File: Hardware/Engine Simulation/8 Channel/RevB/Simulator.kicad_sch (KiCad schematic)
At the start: 69 parts, among them IC1 EL357NB_TA_-G, IC2 EL357NB_TA_-G, J1 Conn_02x20_Counter_Clockwise, J2 Conn_01x08, J3 Conn_01x08, J4 Conn_01x04, J5 Conn_01x04, J6 Conn_01x04, J7 Conn_01x10, J8 Conn_01x03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

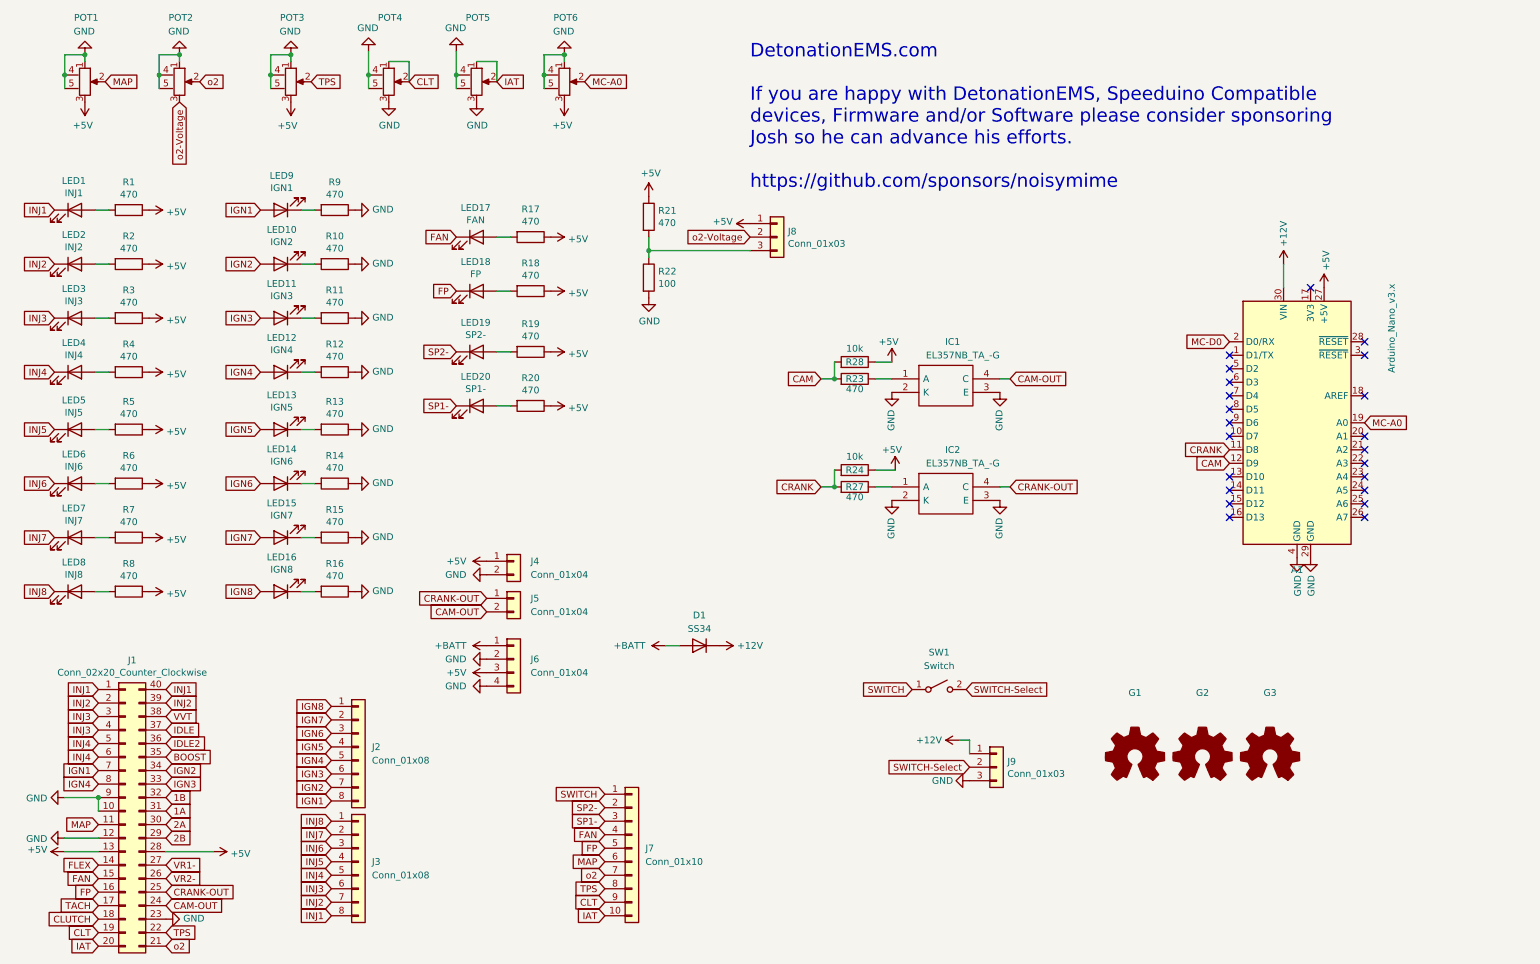
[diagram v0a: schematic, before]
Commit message: Engine Simulator Upload Revision Correcton
Minor changes were made to RevB and uploaded as RevC by mistake. RevB minor layout changes for ease of use. Protection Zener added. Label correction.
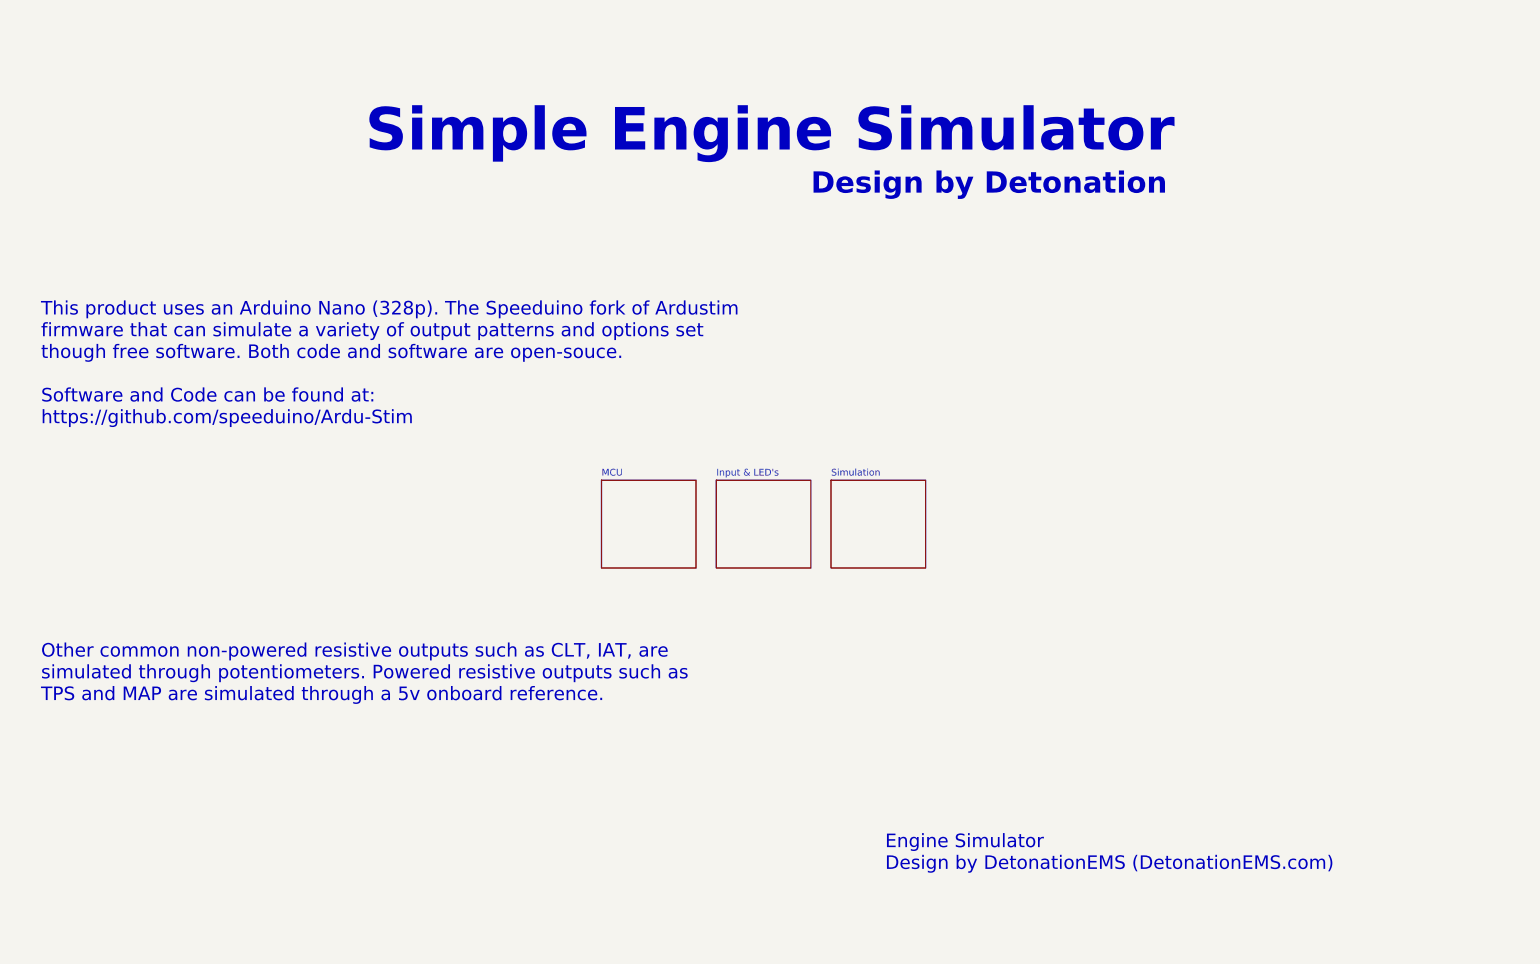
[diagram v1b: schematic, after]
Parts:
- removed A1: Arduino_Nano_v3.x, Module:Arduino_Nano, symbol MCU_Module:Arduino_Nano_v3.x
- removed D1: SS34, Diode_SMD:D_SOD-123, symbol Device:D
- removed G1: Logo_Open_Hardware_Small, Detonation-Logos:Design by 30mm, symbol Graphic:Logo_Open_Hardware_Small
- removed G2: Logo_Open_Hardware_Small, Detonation-Logos:SpeeduinoCompatible-17mm, symbol Graphic:Logo_Open_Hardware_Small
- removed G3: Logo_Open_Hardware_Small, Symbol:OSHW-Logo2_7.3x6mm_SilkScreen, symbol Graphic:Logo_Open_Hardware_Small
- removed IC1, IC2: EL357NB_TA_-G, Detonation:SOP254P700X200-4N, symbol EL357NB_TA_-G:EL357NB_TA_-G
- removed J1: Conn_02x20_Counter_Clockwise, Connector_Automotive:IDC-Header_2x20_P2.54mm_Vertical_Speeduino, symbol Pre_Ignition-rescue:Conn_02x20_Counter_Clockwise-Connector_Generic
- removed J2, J3: Conn_01x08, TerminalBlock_Phoenix:TerminalBlock_Phoenix_PT-1,5-8-3.5-H_1x08_P3.50mm_Horizontal, symbol Connector_Generic:Conn_01x08
- removed J4, J5: Conn_01x04, TerminalBlock_Phoenix:TerminalBlock_Phoenix_PT-1,5-2-3.5-H_1x02_P3.50mm_Horizontal, symbol Connector_Generic:Conn_01x02
- removed J6: Conn_01x04, TerminalBlock_Phoenix:TerminalBlock_Phoenix_PT-1,5-4-3.5-H_1x04_P3.50mm_Horizontal, symbol Connector_Generic:Conn_01x04
- removed J7: Conn_01x10, TerminalBlock_Phoenix:TerminalBlock_Phoenix_PT-1,5-10-3.5-H_1x10_P3.50mm_Horizontal, symbol Connector_Generic:Conn_01x10
- removed J8, J9: Conn_01x03, Detonation:3-PinSwitch, symbol Connector_Generic:Conn_01x03
- removed LED1: INJ1, LED_SMD:LED_0603_1608Metric, symbol Device:LED
- removed LED10: IGN2, LED_SMD:LED_0603_1608Metric, symbol Device:LED
- removed LED11: IGN3, LED_SMD:LED_0603_1608Metric, symbol Device:LED
- removed LED12: IGN4, LED_SMD:LED_0603_1608Metric, symbol Device:LED
- removed LED13: IGN5, LED_SMD:LED_0603_1608Metric, symbol Device:LED
- removed LED14: IGN6, LED_SMD:LED_0603_1608Metric, symbol Device:LED
- removed LED15: IGN7, LED_SMD:LED_0603_1608Metric, symbol Device:LED
- removed LED16: IGN8, LED_SMD:LED_0603_1608Metric, symbol Device:LED
- removed LED17: FAN, LED_SMD:LED_0603_1608Metric, symbol Device:LED
- removed LED18: FP, LED_SMD:LED_0603_1608Metric, symbol Device:LED
- removed LED19: SP2-, LED_SMD:LED_0603_1608Metric, symbol Device:LED
- removed LED2: INJ2, LED_SMD:LED_0603_1608Metric, symbol Device:LED
- removed LED20: SP1-, LED_SMD:LED_0603_1608Metric, symbol Device:LED
- removed LED3: INJ3, LED_SMD:LED_0603_1608Metric, symbol Device:LED
- removed LED4: INJ4, LED_SMD:LED_0603_1608Metric, symbol Device:LED
- removed LED5: INJ5, LED_SMD:LED_0603_1608Metric, symbol Device:LED
- removed LED6: INJ6, LED_SMD:LED_0603_1608Metric, symbol Device:LED
- removed LED7: INJ7, LED_SMD:LED_0603_1608Metric, symbol Device:LED
- removed LED8: INJ8, LED_SMD:LED_0603_1608Metric, symbol Device:LED
- removed LED9: IGN1, LED_SMD:LED_0603_1608Metric, symbol Device:LED
- removed POT1: IAT, MyLibs:RV09AF4020KB10K, symbol Detonation:Pot-10k
- removed POT2: CLT, MyLibs:RV09AF4020KB10K, symbol Detonation:Pot-10k
- removed POT3: MAP/SP1, MyLibs:RV09AF4020KB10K, symbol Detonation:Pot-10k
- removed POT4: TPS, MyLibs:RV09AF4020KB10K, symbol Detonation:Pot-10k
- removed POT5: o2, MyLibs:RV09AF4020KB10K, symbol Detonation:Pot-10k
- removed POT6: RPM, MyLibs:RV09AF4020KB10K, symbol Detonation:Pot-10k
- removed R1, R10, R11, R12, R13, R14, R15, R16, R17, R18, R19, R2, R20, R21, R23, R27, R3, R4, R5, R6, R7, R8, R9: 470, Resistor_SMD:R_0603_1608Metric, symbol Device:R
- removed R22: 100, Resistor_SMD:R_0603_1608Metric, symbol Device:R
- removed R24, R28: 10k, Resistor_SMD:R_0603_1608Metric, symbol Device:R
- removed SW1: Switch, Button_Switch_THT:SW_PUSH_6mm_H9.5mm, symbol Switch:SW_SPST
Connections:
- no-connect marks 22 -> 0
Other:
- added sheet Input & LED's (input.kicad_sch)
- added sheet MCU (mcu.kicad_sch)
- added sheet Simulation (simulation.kicad_sch)
- note added: "Design by Detonation"
- note added: "Engine Simulator Design by DetonationEMS (DetonationEMS.com)"
- note added: "Other common non-powered resistive outputs such as CLT, IAT, are simulated through potentiometers. Powered resistive outputs such as TPS and MAP are simulated through a 5v onboard reference."
- note added: "Simple Engine Simulator"
- note added: "This product uses an Arduino Nano (328p). The Speeduino fork of Ardustim firmware that can simulate a variety of output patterns and options set though free software. Both code and software are open-souce. Software and Code can be found at: https://github.com/speeduino/Ardu-Stim"
- note removed: "DetonationEMS.com If you are happy with DetonationEMS, Speeduino Compatible devices, Firmware and/or Software please consider sponsoring Josh so he can advance his efforts. https://github.com/sponsors/noisymime"

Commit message: Structure Update
MX2 - RevB Upload
MX4B-2 - KiCad Version update (no changes)
MX4C - Organized Schematic, Minor layout change
Engine Simulator 8 Channel - Organized Schematic (no changes)
PMAP-M - Map Sensor Breakout for MX4C
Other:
- note added: "© 2023 DetonationEMS (Aaron S.)"
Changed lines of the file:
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@@
   (title_block
     (title "Engine Simulator")
-    (date "2023-04-09")
-    (rev "Production A")
+    (date "2023-06-15")
+    (rev "Production B")
     (company "DetonationEMS")
   )
@@
     (effects (font (size 2.54 2.54)) (justify left bottom))
   )
-  (text "Design by Detonation" (at 165.1 48.26 0)
+  (text "Design by Detonation" (at 165.1 49.53 0)
     (effects (font (size 4 4) (thickness 0.9) bold) (justify left bottom))
   )
@@
     (effects (font (size 2.54 2.54)) (justify left bottom))
   )
+  (text "© 2023 DetonationEMS (Aaron S.)" (at 82.55 48.26 0)
+    (effects (font (size 2.54 2.54)) (justify left bottom))
+  )
